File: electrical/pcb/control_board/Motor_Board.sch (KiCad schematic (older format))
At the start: 100 parts, among them J1 ED2627-ND, J11 S7038-ND, J12 PEC10DAAN, J13 XT60-F, J14 ED2989-ND-USB, J15 XT60-F, J16 XT60-F, J17 Molex_172675-0613, J18 Molex_172675-0613, J19 Molex_172675-0613, J2 ED2627-ND, J20 Molex_172675-0613, J21 Molex_172675-0613, J22 Molex_172675-0613, J23 Molex_172675-0613, J24 Molex_172675-0613, J25 Molex_172675-0613, J26 Molex_172675-0613, J28 XT60-F, J29 XT60-F, J3 ED2627-ND, J30 XT60-F, J33 ina260_Vin, J34 ina260_8pin, J4 ED2627-ND, J5 ED2627-ND, J9 S7038-ND, M1 Mounting_Holes, T1 test_point, T10 test_point, T11 test_point, T12 test_point, T13 test_point, T14 test_point, T15 test_point, T16 test_point, T17 test_point, T18 test_point, T19 test_point, T2 test_point, T20 test_point, T21 test_point, T3 test_point, T4 test_point, T5 test_point, T6 test_point, T7 test_point, T8 test_point, T9 test_point, U1 LM358-N, U2 LM358-N, y1 rover_silkscreen

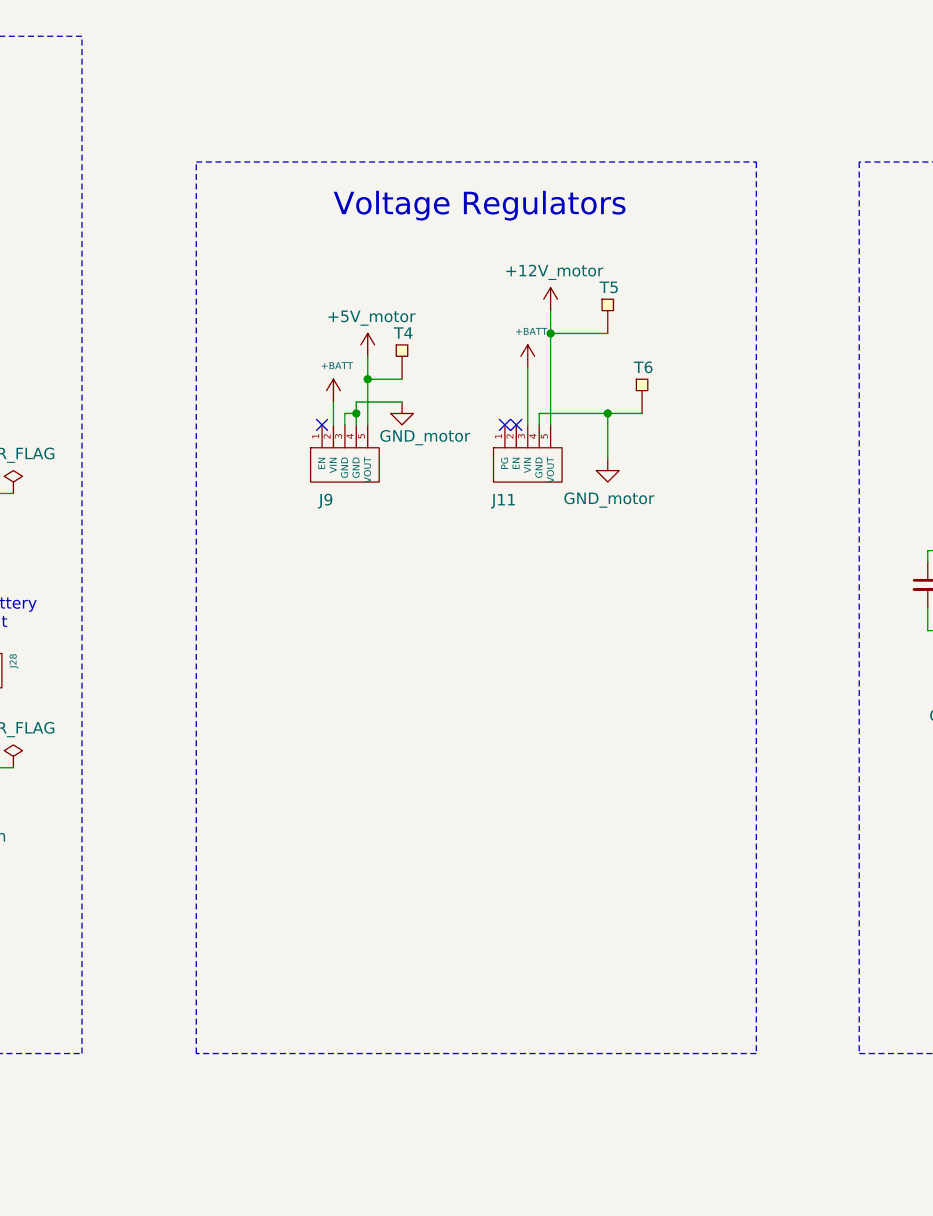
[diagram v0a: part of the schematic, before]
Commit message: Adding headers for connecting servo controller board
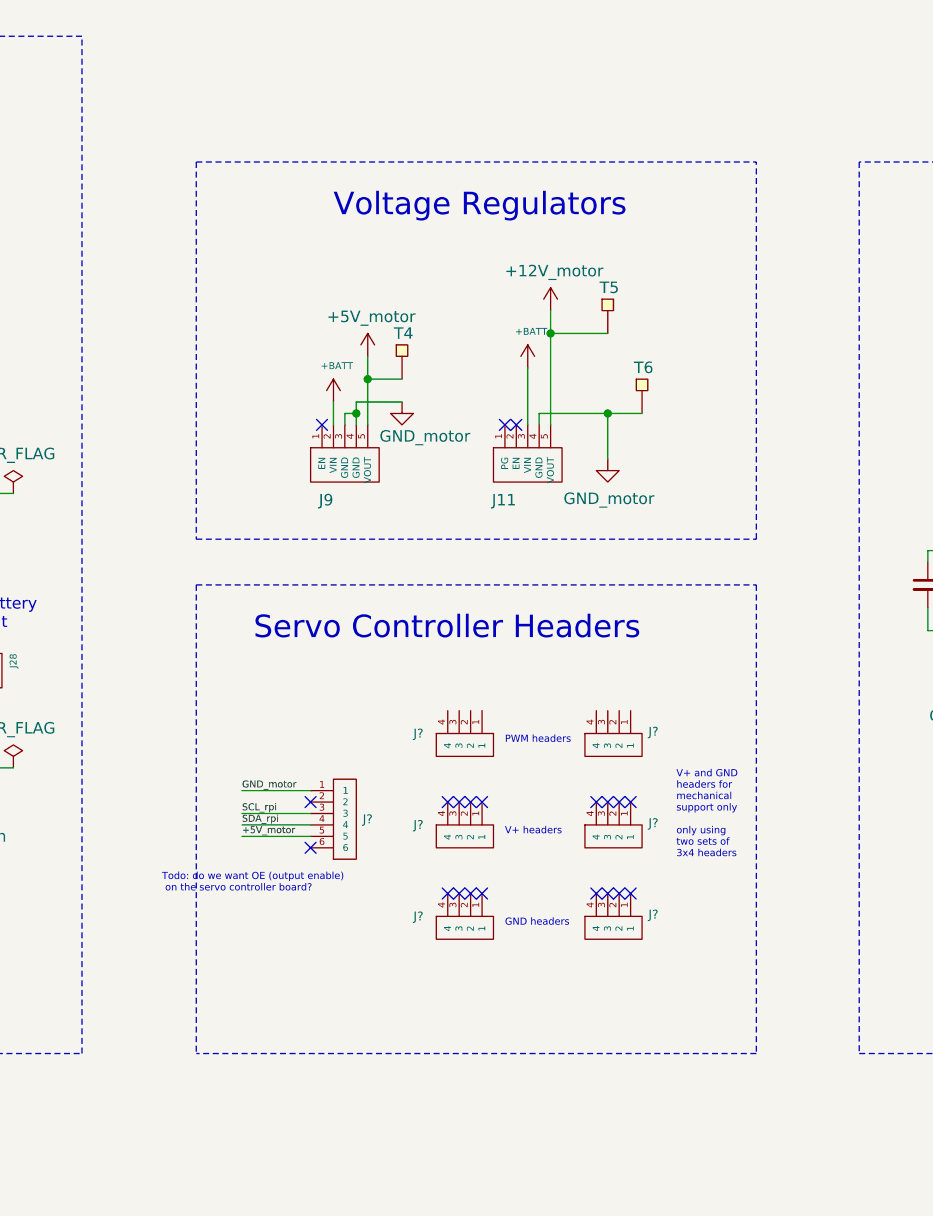
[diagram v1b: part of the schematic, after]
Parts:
- added J?: PPTC061LFBN-RC, symbol JPL_Robotics_Lib:PPTC061LFBN-RC
- added J? (x6): PPTC041LFBN-RC, symbol JPL_Robotics_Lib:PPTC041LFBN-RC
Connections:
- wire segments 399 -> 403
- no-connect marks 101 -> 119
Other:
- note added: "GND headers"
- note added: "PWM headers"
- note added: "Servo Controller Headers"
- note added: "Todo: do we want OE (output enable)\n on the servo controller board?"
- note added: "V+ and GND \nheaders for \nmechanical \nsupport only\n\nonly using\ntwo sets of \n3x4 headers"
- note added: "V+ headers"
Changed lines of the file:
@@
 	8300 5450 8300 9350
-Wire Notes Line style solid rgb(0, 0, 0)
-	7850 5450 7850 9350
-Wire Notes Line style solid rgb(0, 0, 0)
-	7850 9350 5400 9350
-Wire Notes Line style solid rgb(0, 0, 0)
-	5400 9350 5400 5450
 Wire Notes Line style solid rgb(0, 0, 0)
 	5400 5450 7850 5450
@@
 Wire Wire Line
 	3300 8500 3400 8500
-Text Label 3650 8500 0    50   ~ 0
-+5V_motor
 Wire Wire Line
 	3650 8500 4050 8500
@@
 Wire Wire Line
 	1600 6600 2750 6600
+Wire Notes Line
+	5400 5450 5400 7100
+Wire Notes Line
+	5400 7100 7850 7100
+Wire Notes Line
+	7850 7100 7850 5450
+Wire Notes Line
+	5400 7300 7850 7300
+Wire Notes Line
+	7850 7300 7850 9350
+Wire Notes Line
+	7850 9350 5400 9350
+Text Notes 5650 7550 0    98   ~ 0
+Servo Controller Headers
+$Comp
+L JPL_Robotics_Lib:PPTC061LFBN-RC J?
+U 1 1 60BBA8E7
+P 6000 8500
+F 0 "J?" H 6128 8675 39  0000 L CNN
+F 1 "PPTC061LFBN-RC" H 6050 8950 50  0001 C CNN
+F 2 "" H 6150 8800 50  0001 C CNN
+F 3 "" H 6150 8800 50  0001 C CNN
+	1    6000 8500
+	1    0    0    -1
+$EndComp
+$Comp
+L JPL_Robotics_Lib:PPTC041LFBN-RC J?
+U 1 1 60BBCE9F
+P 6450 7950
+F 0 "J?" V 6450 7850 39  0000 L CNN
+F 1 "PPTC041LFBN-RC" H 6500 8300 50  0001 C CNN
+F 2 "" H 6600 8150 50  0001 C CNN
+F 3 "" H 6600 8150 50  0001 C CNN
+	1    6450 7950
+	0    1    1    0
+$EndComp
+$Comp
+L JPL_Robotics_Lib:PPTC041LFBN-RC J?
+U 1 1 60BBD6E1
+P 6450 8350
+F 0 "J?" V 6450 8250 39  0000 L CNN
+F 1 "PPTC041LFBN-RC" H 6500 8700 50  0001 C CNN
+F 2 "" H 6600 8550 50  0001 C CNN
+F 3 "" H 6600 8550 50  0001 C CNN
+	1    6450 8350
+	0    1    1    0
+$EndComp
+$Comp
+L JPL_Robotics_Lib:PPTC041LFBN-RC J?
+U 1 1 60BBDC32
+P 6450 8750
+F 0 "J?" V 6450 8650 39  0000 L CNN
+F 1 "PPTC041LFBN-RC" H 6500 9100 50  0001 C CNN
+F 2 "" H 6600 8950 50  0001 C CNN
+F 3 "" H 6600 8950 50  0001 C CNN
+	1    6450 8750
+	0    1    1    0
+$EndComp
+$Comp
+L JPL_Robotics_Lib:PPTC041LFBN-RC J?
+U 1 1 60BBE216
+P 7100 7950
+F 0 "J?" V 7092 8228 39  0000 L CNN
+F 1 "PPTC041LFBN-RC" H 7150 8300 50  0001 C CNN
+F 2 "" H 7250 8150 50  0001 C CNN
+F 3 "" H 7250 8150 50  0001 C CNN
+	1    7100 7950
+	0    1    1    0
+$EndComp
+Wire Wire Line
+	5900 8200 5600 8200
+Text Label 5600 8200 0    30   ~ 0
+GND_motor
+Wire Wire Line
+	5900 8300 5600 8300
+Text Label 5600 8300 0    30   ~ 0
+SCL_rpi
+Wire Wire Line
+	5900 8350 5600 8350
+Text Label 5600 8350 0    30   ~ 0
+SDA_rpi
+Wire Wire Line
+	5900 8400 5600 8400
+Text Label 5600 8400 0    30   ~ 0
++5V_motor
+Text Label 3650 8500 0    50   ~ 0
++5V_motor
+NoConn ~ 5900 8450
+NoConn ~ 5900 8250
+Text Notes 5250 8650 0    31   ~ 0
+Todo: do we want OE (output enable)\n on the servo controller board?
+Wire Notes Line
+	5400 7300 5400 9350
+NoConn ~ 6500 8250
+NoConn ~ 6550 8250
+NoConn ~ 6600 8250
+NoConn ~ 6650 8250
+NoConn ~ 6500 8650
+NoConn ~ 6550 8650
+NoConn ~ 6600 8650
+NoConn ~ 6650 8650
+$Comp
+L JPL_Robotics_Lib:PPTC041LFBN-RC J?
+U 1 1 60F4216F
+P 7100 8350
+F 0 "J?" V 7092 8628 39  0000 L CNN
+F 1 "PPTC041LFBN-RC" H 7150 8700 50  0001 C CNN
+F 2 "" H 7250 8550 50  0001 C CNN
+F 3 "" H 7250 8550 50  0001 C CNN
+	1    7100 8350
+	0    1    1    0
+$EndComp
+$Comp
+L JPL_Robotics_Lib:PPTC041LFBN-RC J?
+U 1 1 60F42175
+P 7100 8750
+F 0 "J?" V 7092 9028 39  0000 L CNN
+F 1 "PPTC041LFBN-RC" H 7150 9100 50  0001 C CNN
+F 2 "" H 7250 8950 50  0001 C CNN
+F 3 "" H 7250 8950 50  0001 C CNN
+	1    7100 8750
+	0    1    1    0
+$EndComp
+NoConn ~ 7150 8250
+NoConn ~ 7200 8250
+NoConn ~ 7250 8250
+NoConn ~ 7300 8250
+NoConn ~ 7150 8650
+NoConn ~ 7200 8650
+NoConn ~ 7250 8650
+NoConn ~ 7300 8650
+Text Notes 7500 8500 0    31   ~ 0
+V+ and GND \nheaders for \nmechanical \nsupport only\n\nonly using\ntwo sets of \n3x4 headers
+Text Notes 6750 8400 0    31   ~ 0
+V+ headers
+Text Notes 6750 8800 0    31   ~ 0
+GND headers
+Text Notes 6750 8000 0    31   ~ 0
+PWM headers
 $EndSCHEMATC

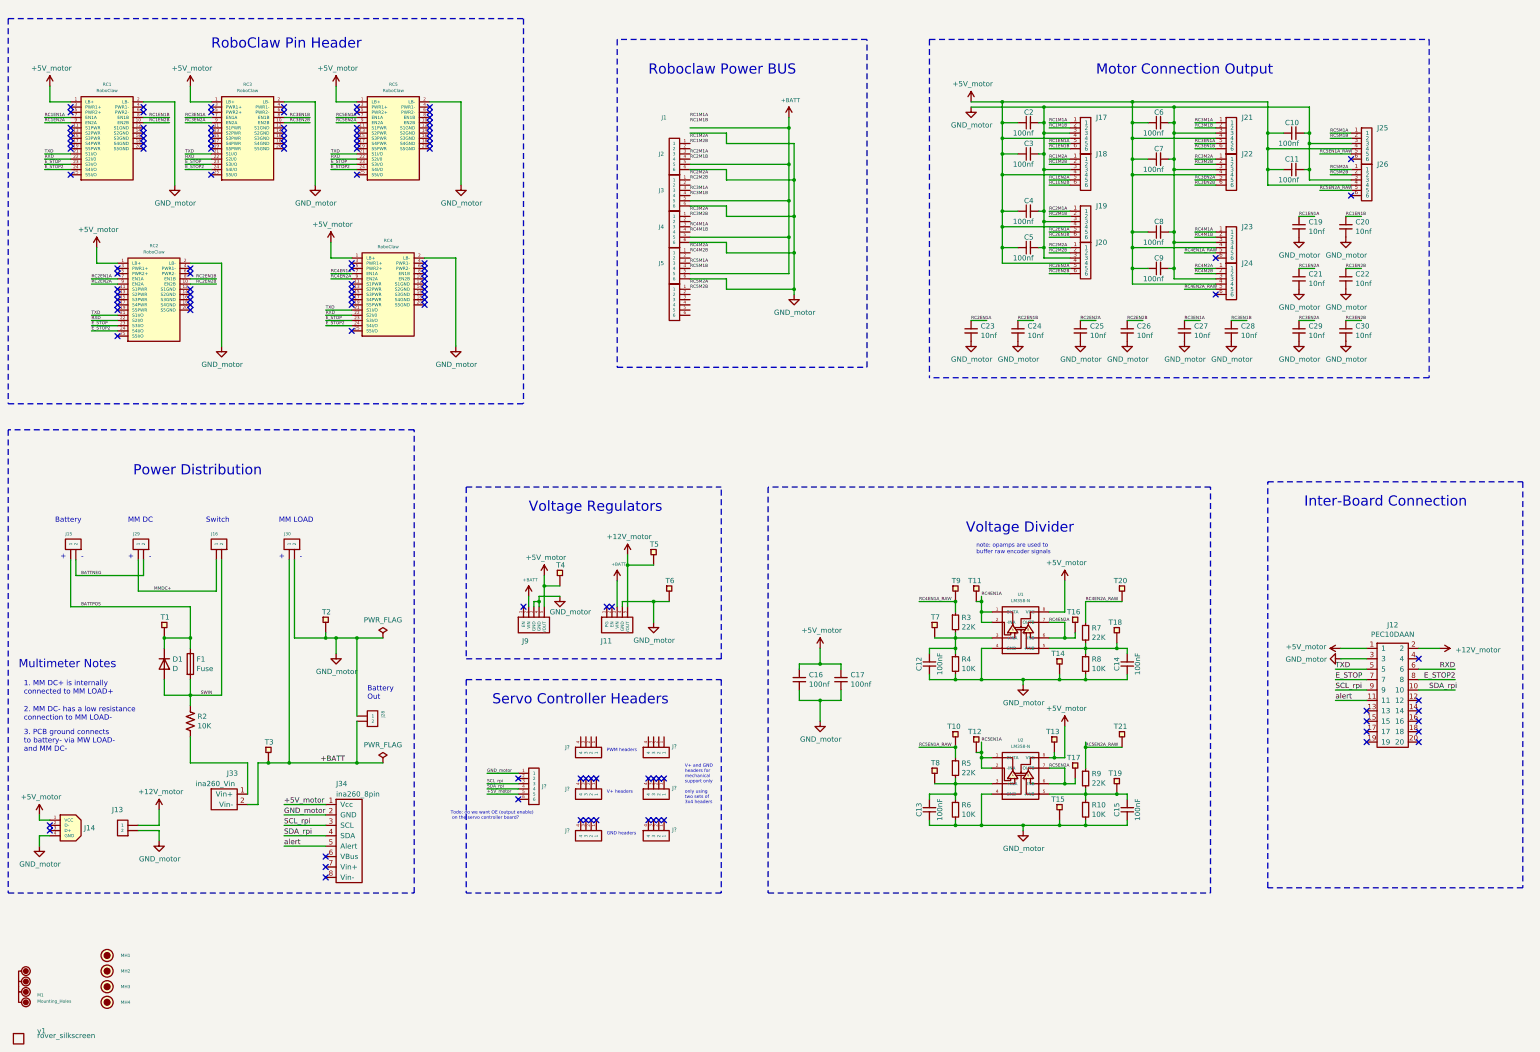
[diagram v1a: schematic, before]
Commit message: Deleting Roboclaw motor controllers 4 and 5 from the schematic, and adding motor connection headers for 4 servos
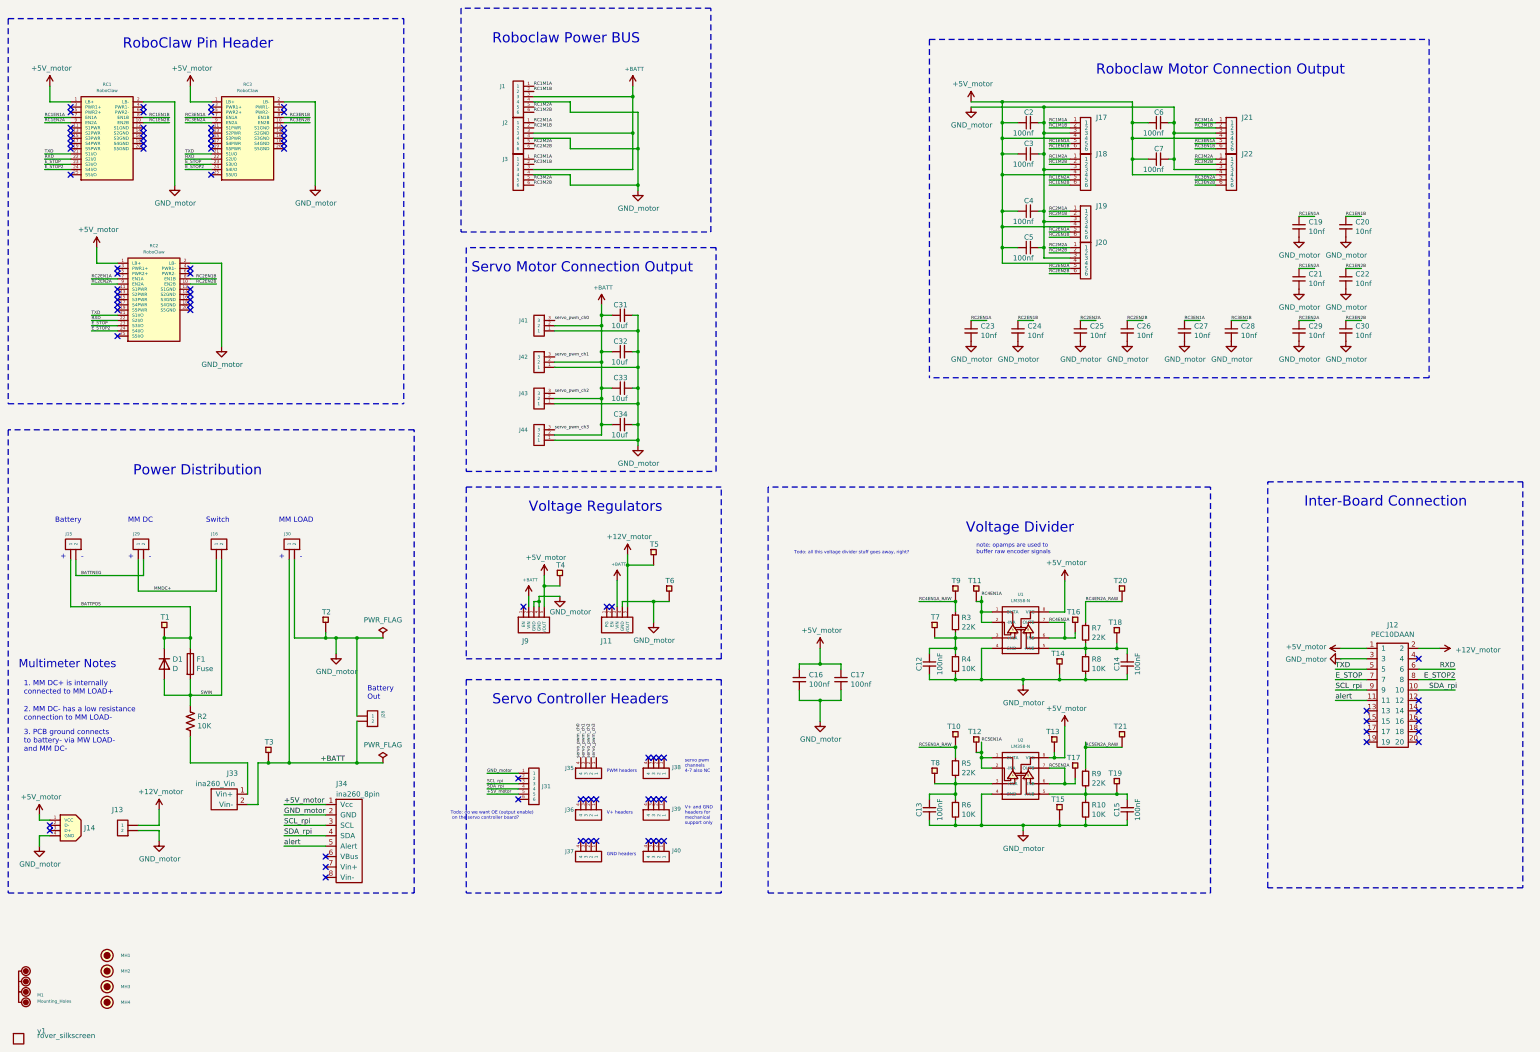
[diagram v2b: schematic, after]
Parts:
- removed C10, C11, C8, C9: 100nf, Resistor_THT:R_Axial_DIN0207_L6.3mm_D2.5mm_P7.62mm_Horizontal, symbol Device:C_Small
- removed J23, J24, J25, J26: Molex_172675-0613, symbol JPL_Robotics_Lib:Molex_172675-0613
- removed J4, J5: ED2627-ND, JPL Robotics:ED2627-ND, symbol JPL_Robotics_Lib:ED2627-ND
- removed RC4, RC5: RoboClaw, JPL Robotics:Roboclaw Mount, symbol JPL_Robotics_Lib:RoboClaw
- added C31, C32, C33, C34: 10uf, Resistor_THT:R_Axial_DIN0207_L6.3mm_D2.5mm_P7.62mm_Horizontal, symbol Device:C_Small
- added J41, J42, J43, J44: PPTC031LFBN-RC, symbol JPL_Robotics_Lib:PPTC031LFBN-RC
- gave numbers to parts that had none: 7
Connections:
- net labels added: servo_pwm_ch0, servo_pwm_ch1, servo_pwm_ch2, servo_pwm_ch3
- net labels removed: RC4M1A, RC4M1B, RC4M2A, RC4M2B, RC5M1A, RC5M1B, RC5M2A, RC5M2B
- wire segments 403 -> 357
- no-connect marks 119 -> 85
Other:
- note added: "Roboclaw Motor Connection Output"
- note added: "Servo Motor Connection Output"
- note added: "Todo: all this voltage divider stuff goes away, right?"
- note added: "V+ and GND \nheaders for \nmechanical \nsupport only"
- note added: "servo pwm\nchannels \n4-7 also NC"
- note removed: "Motor Connection Output"
- note removed: "V+ and GND \nheaders for \nmechanical \nsupport only\n\nonly using\ntwo sets of \n3x4 headers"
- moved on the sheet: J1, J2, J3, J35, J36, J37, J38, J39, J40

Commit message: adding a bunch of todo notes in the schematic
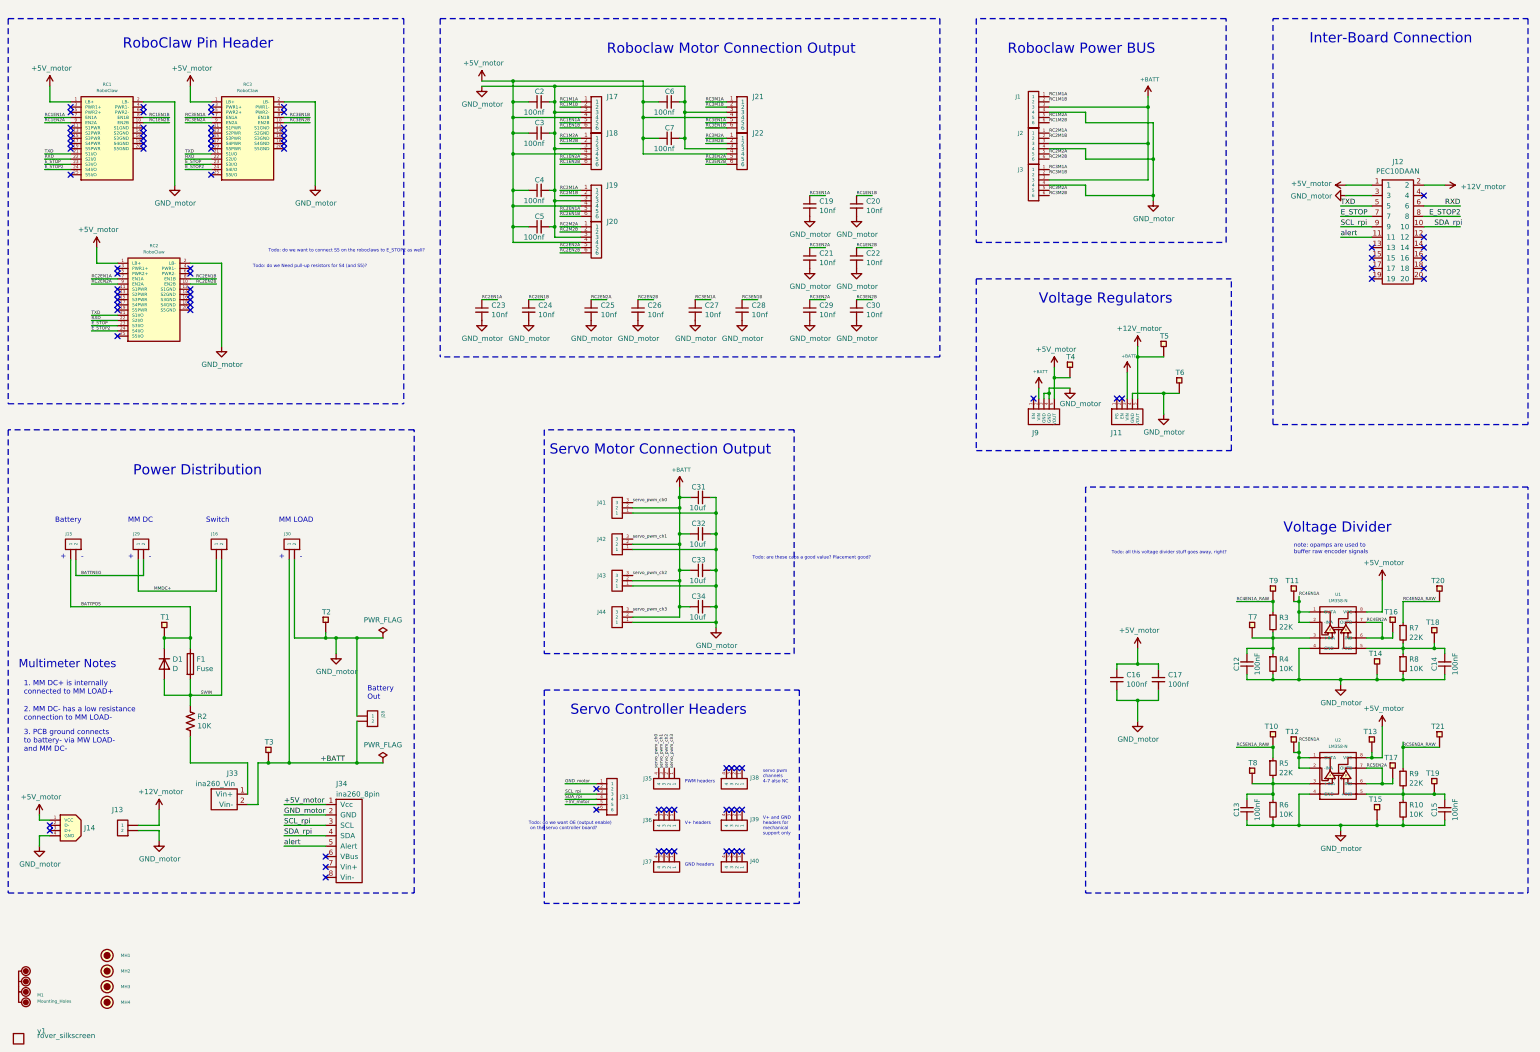
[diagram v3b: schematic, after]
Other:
- note added: "Todo: are these caps a good value? Placement good?"
- note added: "Todo: do we Need pull-up resistors for S4 (and S5)?\n"
- note added: "Todo: do we want to connect S5 on the roboclaws to E_STOP2 as well?\n"
- moved on the sheet: C12, C13, C14, C15, C16, C17, C19, C2, C20, C21, C22, C23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

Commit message: WIP updates for control board after initial review
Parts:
- removed C12, C13, C14, C15: 100nF, Resistor_THT:R_Axial_DIN0207_L6.3mm_D2.5mm_P7.62mm_Horizontal, symbol Device:C_Small
- removed C16, C17: 100nf, Resistor_THT:R_Axial_DIN0207_L6.3mm_D2.5mm_P7.62mm_Horizontal, symbol Device:C_Small
- removed R10, R4, R6, R8: 10K, Resistor_THT:R_Axial_DIN0207_L6.3mm_D2.5mm_P7.62mm_Horizontal, symbol Device:R_Small
- removed R3, R5, R7, R9: 22K, Resistor_THT:R_Axial_DIN0207_L6.3mm_D2.5mm_P7.62mm_Horizontal, symbol Device:R_Small
- removed T10, T11, T12, T13, T14, T15, T16, T17, T18, T19, T20, T21, T7, T8, T9: test_point, TestPoint:TestPoint_Pad_1.0x1.0mm, symbol JPL_Robotics_Lib:test_point
- removed U1, U2: LM358-N, JPL Robotics:AE9986-ND, symbol JPL_Robotics_Lib:LM358-N
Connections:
- net labels removed: RC4EN1A, RC4EN1A_RAW, RC4EN2A, RC4EN2A_RAW, RC5EN1A, RC5EN1A_RAW, RC5EN2A, RC5EN2A_RAW
- wire segments 357 -> 249
- no-connect marks 85 -> 88
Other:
- note removed: "Todo: all this voltage divider stuff goes away, right?"
- note removed: "Voltage Divider"
- note removed: "note: opamps are used to \nbuffer raw encoder signals"
